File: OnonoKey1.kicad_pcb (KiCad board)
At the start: 2 copper layers, 136.9 x 136.4 mm, 95 parts, among them SW00 Switch, SW01 Switch, SW02 Switch, SW03 Switch, SW04 Switch, SW05 Switch, SW06 Switch, SW10 Switch, SW11 Switch, SW12 Switch, SW13 Switch, SW14 Switch, SW15 Switch, SW16 Switch, SW20 Switch, SW21 Switch, SW22 Switch, SW23 Switch, SW24 Switch, SW25 Switch, SW26 Switch, SW30 Switch, SW31 Switch, SW32 Switch, SW33 Switch, SW34 Switch, SW35 Switch, SW36 Switch, SW40 Switch, SW41 Switch, SW42 Switch, SW43 Switch, SW44 Switch, SW45 Switch, SW46 Switch, SW50 Switch, SW51 Switch, SW52 Switch, SW53 Switch, SW54 Switch, SW55 Switch, SW56 Switch, U1 RP2040_Zero, U2 TRRS Front, U3 TRRS Back

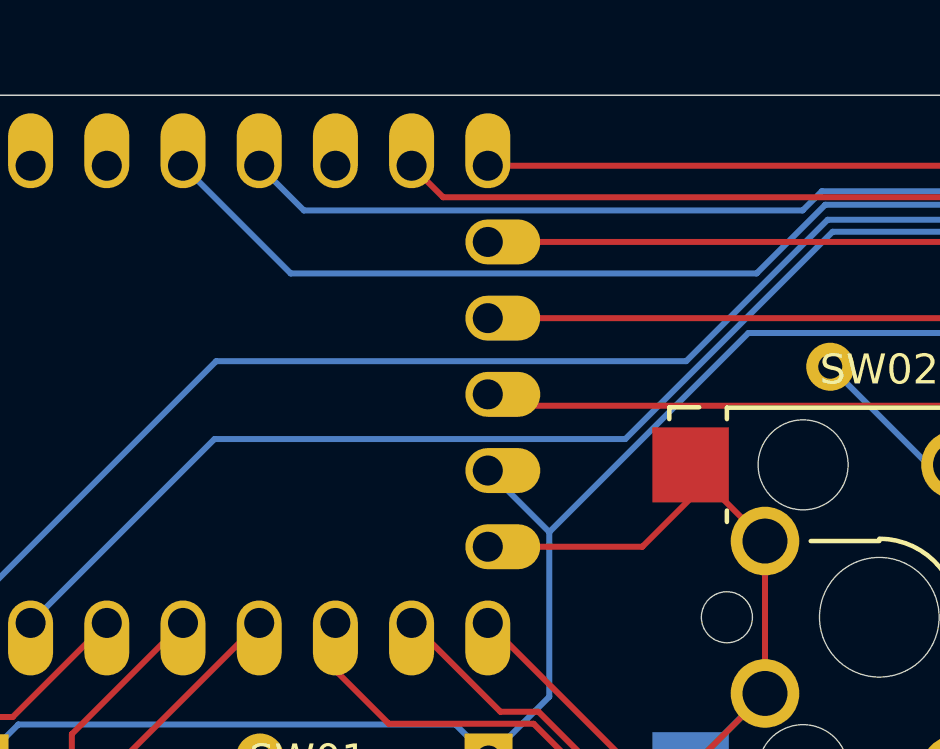
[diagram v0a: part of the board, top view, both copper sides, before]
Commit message: Added two 2.7 holes for buttons access on upside down RP2040 Zero. Generated new gerbers for it
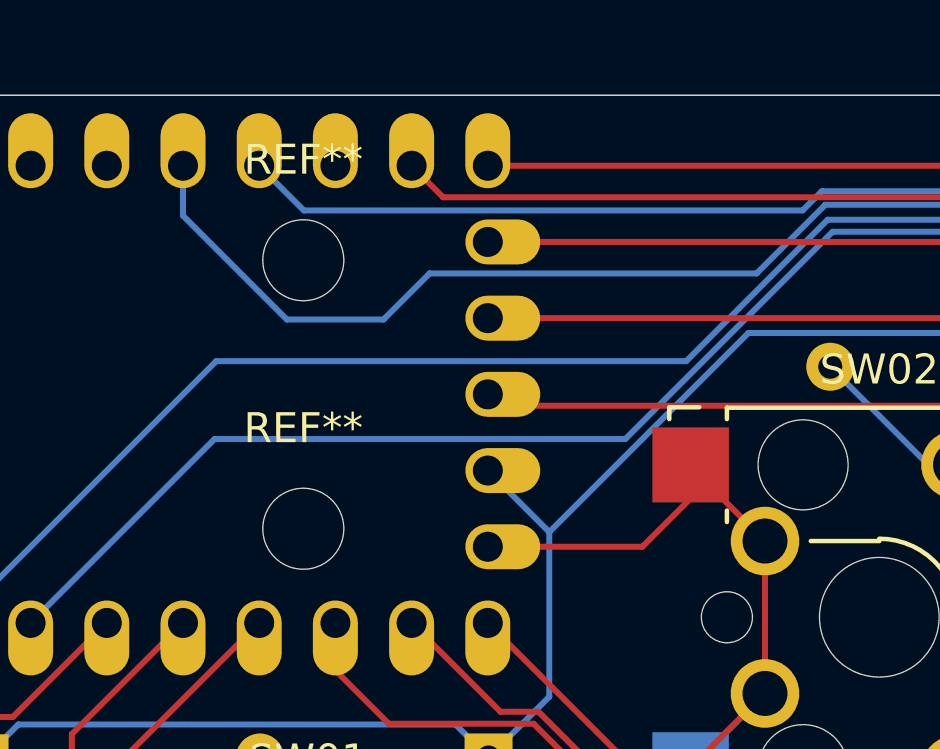
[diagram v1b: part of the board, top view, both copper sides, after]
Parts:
- added REF**: MountingHole_2.7mm_M2.5_DIN965, MountingHole:MountingHole_2.7mm_M2.5_DIN965, F.Cu at (60.5, 45.0)
- added REF**: MountingHole_2.7mm_M2.5_DIN965, MountingHole:MountingHole_2.7mm_M2.5_DIN965, F.Cu at (60.5, 36.1)
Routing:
- net /TX1: track 115.8 -> 118.1 mm
